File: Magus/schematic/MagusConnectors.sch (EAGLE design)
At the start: 47 parts, among them IC3 RC4560, J1 POWER_JACK, U1 REG_S9V11F5, U2 REG_U3V12F12, U3 ICL7660, X2 1503_09, X4 1503_09, X5 1503_09

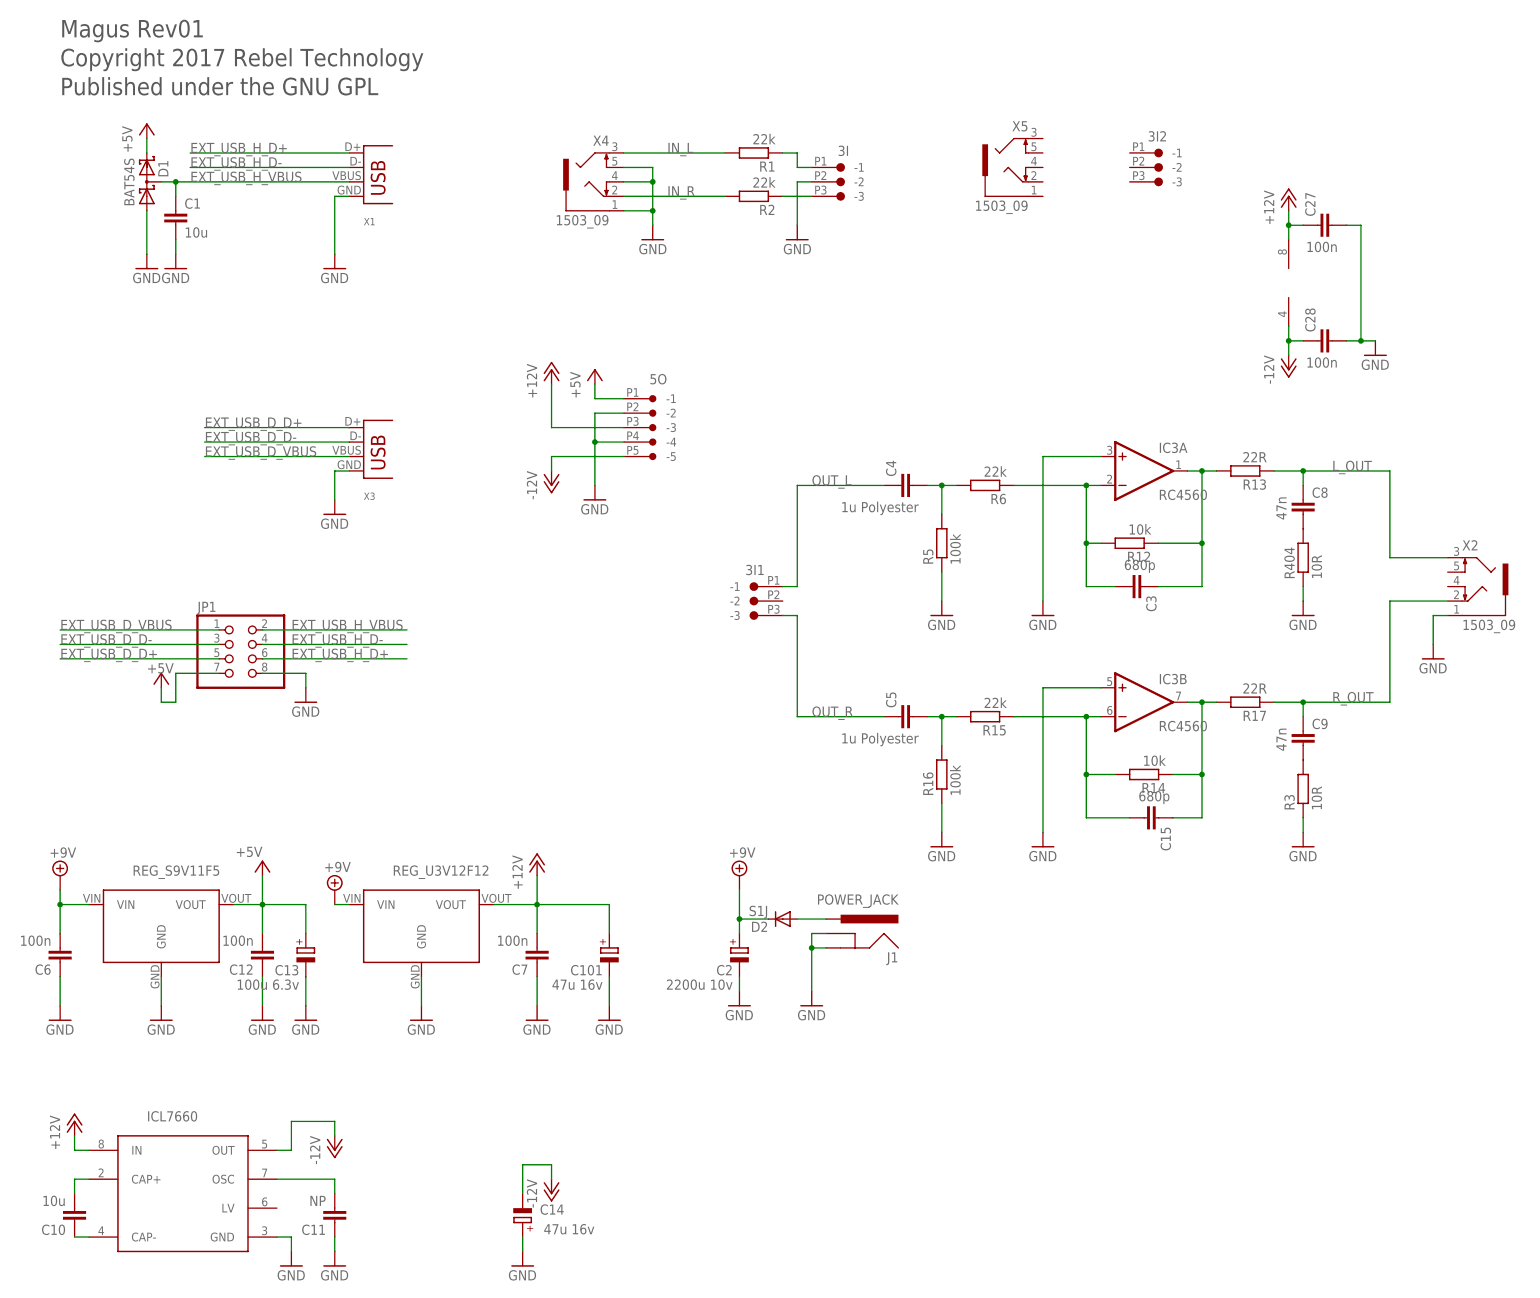
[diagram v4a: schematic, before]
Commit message: updated connectors board
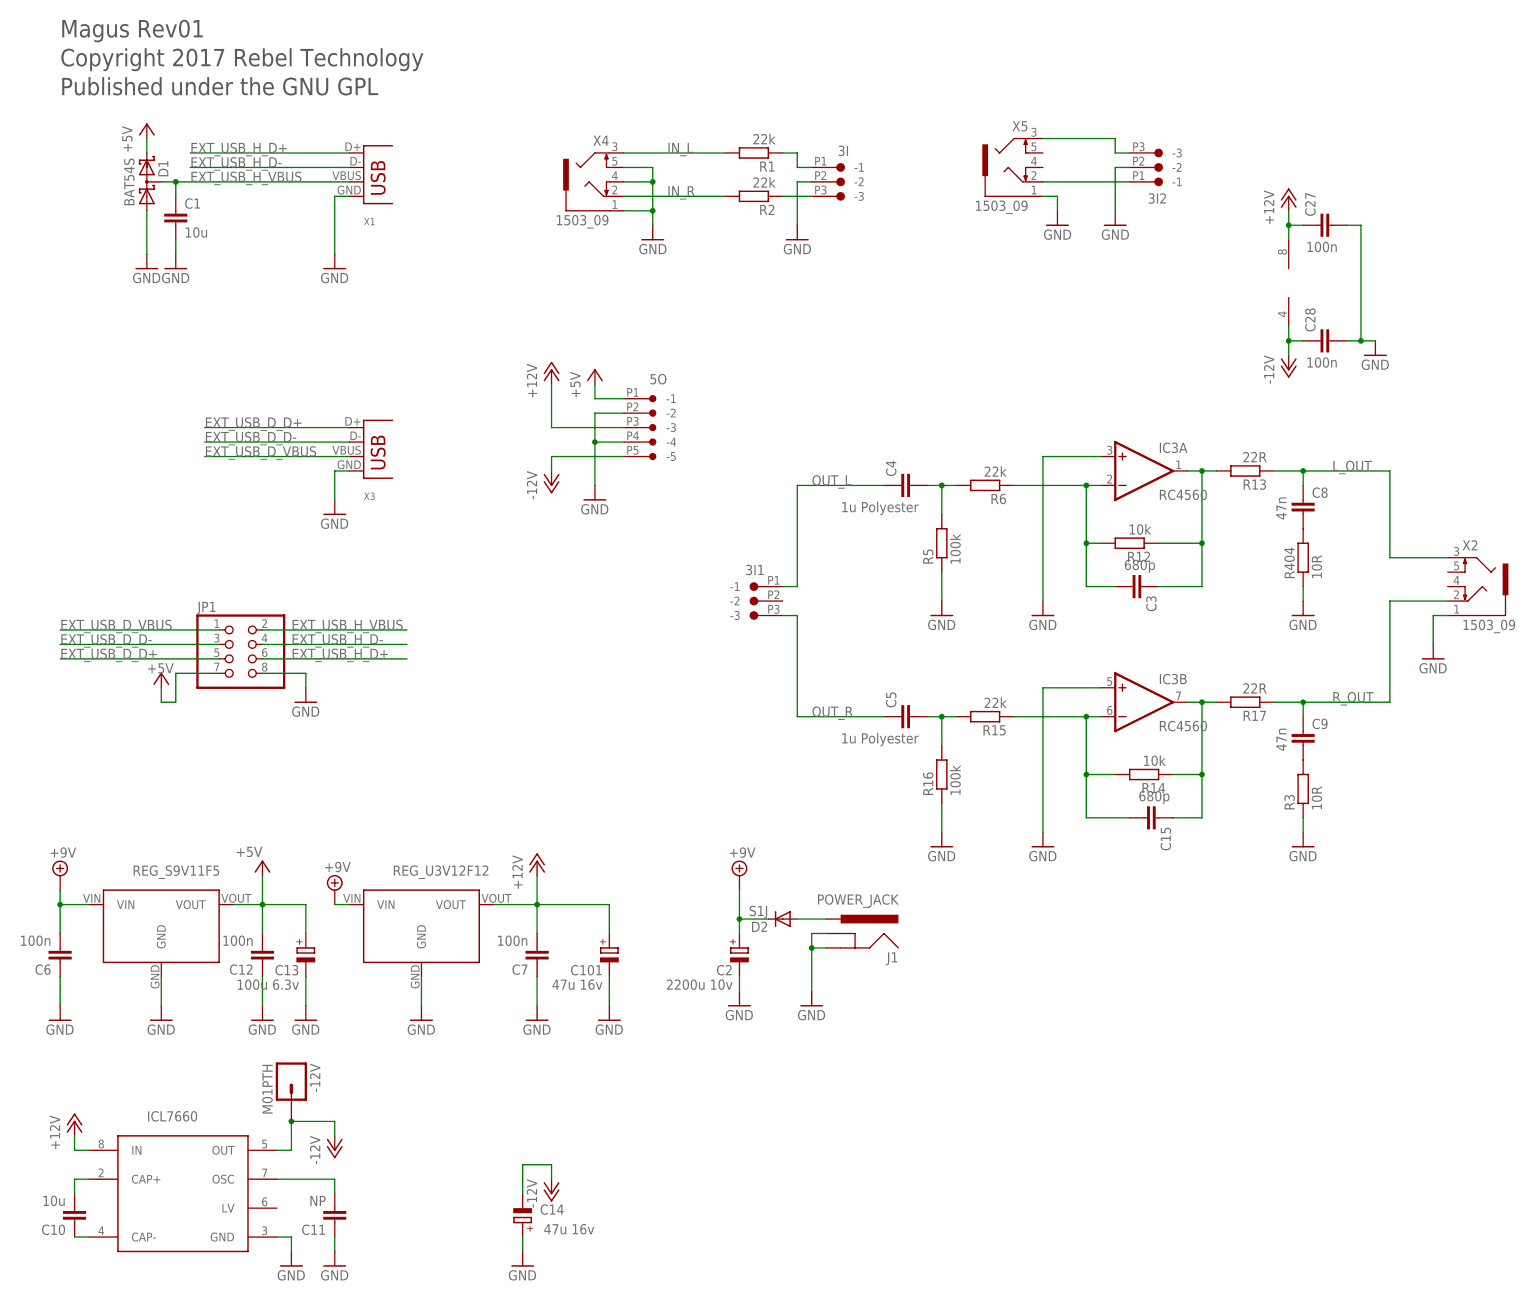
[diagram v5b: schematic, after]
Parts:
- added -12V: M01PTH, SparkFun:M01PTH
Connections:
- new net N$14: 3I2.-3, X5.3
- new net N$7: 3I2.-1, X5.2
- net -12V: now also -12V.1
- net GND: now also 3I2.-2, X5.1
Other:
- moved on the sheet: 3I2
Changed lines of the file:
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@@
 <part name="X5" library="con-lumberg" deviceset="1503_09" device=""/>
 <part name="3I2" library="Rebel" deviceset="CON-JST_PH_3W" device=""/>
+<part name="-12V" library="SparkFun" deviceset="M01" device="PTH"/>
+<part name="GND16" library="supply1" deviceset="GND" device=""/>
+<part name="GND17" library="supply1" deviceset="GND" device=""/>
 </parts>
 <sheets>
@@
 </instance>
 <instance part="X5" gate="G$1" x="172.72" y="96.52" rot="MR0"/>
-<instance part="3I2" gate="G$1" x="193.04" y="99.06" rot="MR0"/>
+<instance part="3I2" gate="G$1" x="193.04" y="93.98" rot="R180"/>
+<instance part="-12V" gate="G$1" x="45.72" y="-63.5" rot="R270"/>
+<instance part="GND16" gate="1" x="190.5" y="86.36" rot="MR0"/>
+<instance part="GND17" gate="1" x="180.34" y="86.36" rot="MR0"/>
 </instances>
 <busses>
@@
 <wire x1="86.36" y1="-91.44" x2="86.36" y2="-93.98" width="0.1524" layer="91"/>
 </segment>
+<segment>
+<pinref part="3I2" gate="G$1" pin="-2"/>
+<pinref part="GND16" gate="1" pin="GND"/>
+<wire x1="193.04" y1="96.52" x2="190.5" y2="96.52" width="0.1524" layer="91"/>
+<wire x1="190.5" y1="96.52" x2="190.5" y2="88.9" width="0.1524" layer="91"/>
+</segment>
+<segment>
+<pinref part="X5" gate="G$1" pin="1"/>
+<wire x1="177.8" y1="91.44" x2="180.34" y2="91.44" width="0.1524" layer="91"/>
+<pinref part="GND17" gate="1" pin="GND"/>
+<wire x1="180.34" y1="91.44" x2="180.34" y2="88.9" width="0.1524" layer="91"/>
+</segment>
 </net>
 <net name="IN_L" class="0">
@@
 <wire x1="45.72" y1="-71.12" x2="53.34" y2="-71.12" width="0.1524" layer="91"/>
 <wire x1="53.34" y1="-71.12" x2="53.34" y2="-73.66" width="0.1524" layer="91"/>
+<pinref part="-12V" gate="G$1" pin="1"/>
+<junction x="45.72" y="-71.12"/>
 </segment>
 </net>
@@
 </segment>
 </net>
+<net name="N$14" class="0">
+<segment>
+<wire x1="190.5" y1="99.06" x2="190.5" y2="101.6" width="0.1524" layer="91"/>
+<pinref part="X5" gate="G$1" pin="3"/>
+<wire x1="190.5" y1="101.6" x2="177.8" y2="101.6" width="0.1524" layer="91"/>
+<pinref part="3I2" gate="G$1" pin="-3"/>
+<wire x1="193.04" y1="99.06" x2="190.5" y2="99.06" width="0.1524" layer="91"/>
+</segment>
+</net>
+<net name="N$7" class="0">
+<segment>
+<pinref part="3I2" gate="G$1" pin="-1"/>
+<pinref part="X5" gate="G$1" pin="2"/>
+<wire x1="193.04" y1="93.98" x2="177.8" y2="93.98" width="0.1524" layer="91"/>
+</segment>
+</net>

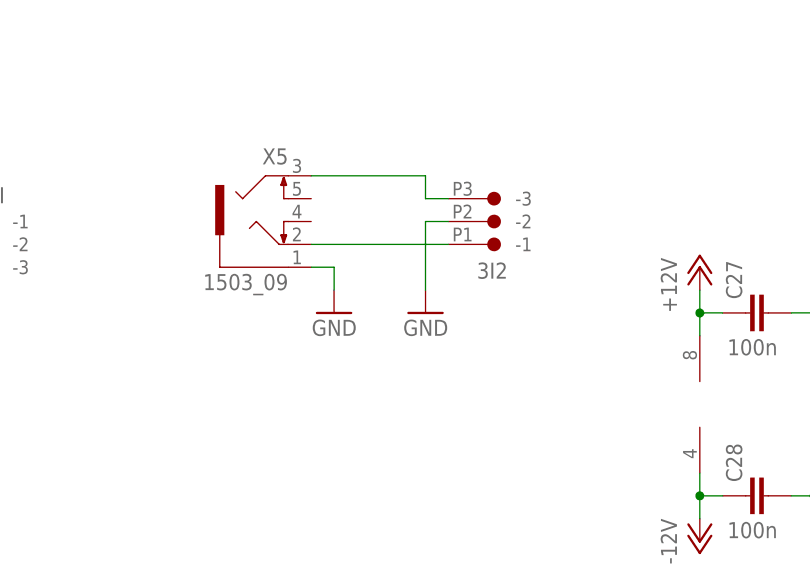
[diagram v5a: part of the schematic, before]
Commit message: disconnected EXT header sleeve / pin 2 from gnd
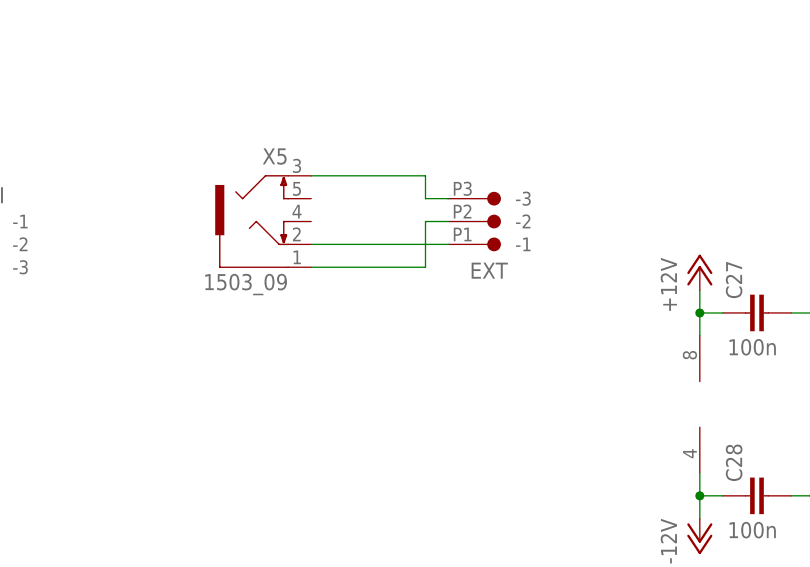
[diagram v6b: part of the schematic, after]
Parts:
- renumbered 3I2 to EXT
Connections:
- new net N$15: EXT.-2, X5.1
- net GND: no longer EXT.-2, X5.1
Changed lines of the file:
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@@
 <?xml version="1.0" encoding="utf-8"?>
 <!DOCTYPE eagle SYSTEM "eagle.dtd">
-<eagle version="9.0.0">
+<eagle version="8.7.1">
 <drawing>
 <settings>
@@
 <part name="C15" library="Rebel" deviceset="C-EU" device="C0603" value="680p"/>
 <part name="X5" library="con-lumberg" deviceset="1503_09" device=""/>
-<part name="3I2" library="Rebel" deviceset="CON-JST_PH_3W" device=""/>
+<part name="EXT" library="Rebel" deviceset="CON-JST_PH_3W" device=""/>
 <part name="-12V" library="SparkFun" deviceset="M01" device="PTH"/>
-<part name="GND16" library="supply1" deviceset="GND" device=""/>
-<part name="GND17" library="supply1" deviceset="GND" device=""/>
 </parts>
 <sheets>
@@
 </instance>
 <instance part="X5" gate="G$1" x="172.72" y="96.52" rot="MR0"/>
-<instance part="3I2" gate="G$1" x="193.04" y="93.98" rot="R180"/>
+<instance part="EXT" gate="G$1" x="193.04" y="93.98" rot="R180"/>
 <instance part="-12V" gate="G$1" x="45.72" y="-63.5" rot="R270"/>
-<instance part="GND16" gate="1" x="190.5" y="86.36" rot="MR0"/>
-<instance part="GND17" gate="1" x="180.34" y="86.36" rot="MR0"/>
 </instances>
 <busses>
@@
 <wire x1="86.36" y1="-91.44" x2="86.36" y2="-93.98" width="0.1524" layer="91"/>
 </segment>
-<segment>
-<pinref part="3I2" gate="G$1" pin="-2"/>
-<pinref part="GND16" gate="1" pin="GND"/>
-<wire x1="193.04" y1="96.52" x2="190.5" y2="96.52" width="0.1524" layer="91"/>
-<wire x1="190.5" y1="96.52" x2="190.5" y2="88.9" width="0.1524" layer="91"/>
-</segment>
-<segment>
-<pinref part="X5" gate="G$1" pin="1"/>
-<wire x1="177.8" y1="91.44" x2="180.34" y2="91.44" width="0.1524" layer="91"/>
-<pinref part="GND17" gate="1" pin="GND"/>
-<wire x1="180.34" y1="91.44" x2="180.34" y2="88.9" width="0.1524" layer="91"/>
-</segment>
 </net>
 <net name="IN_L" class="0">
@@
 <pinref part="X5" gate="G$1" pin="3"/>
 <wire x1="190.5" y1="101.6" x2="177.8" y2="101.6" width="0.1524" layer="91"/>
-<pinref part="3I2" gate="G$1" pin="-3"/>
+<pinref part="EXT" gate="G$1" pin="-3"/>
 <wire x1="193.04" y1="99.06" x2="190.5" y2="99.06" width="0.1524" layer="91"/>
 </segment>
@@
 <net name="N$7" class="0">
 <segment>
-<pinref part="3I2" gate="G$1" pin="-1"/>
+<pinref part="EXT" gate="G$1" pin="-1"/>
 <pinref part="X5" gate="G$1" pin="2"/>
 <wire x1="193.04" y1="93.98" x2="177.8" y2="93.98" width="0.1524" layer="91"/>
 </segment>
 </net>
+<net name="N$15" class="0">
+<segment>
+<pinref part="EXT" gate="G$1" pin="-2"/>
+<wire x1="193.04" y1="96.52" x2="190.5" y2="96.52" width="0.1524" layer="91"/>
+<pinref part="X5" gate="G$1" pin="1"/>
+<wire x1="177.8" y1="91.44" x2="190.5" y2="91.44" width="0.1524" layer="91"/>
+<wire x1="190.5" y1="91.44" x2="190.5" y2="96.52" width="0.1524" layer="91"/>
+</segment>
+</net>
